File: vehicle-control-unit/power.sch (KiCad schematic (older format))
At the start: 0 parts

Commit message: Finish VCU schematic
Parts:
- added C1: 10u, symbol Device:CP
- added C2: 22u, symbol Device:CP
- added J13: Conn_01x02_Male, symbol Connector:Conn_01x02_Male
- added JP6: Jumper_3_Bridged12, symbol earth-rover-symbols:Jumper_3_Bridged12
- added R16: 820E, symbol Device:R
- added R17: 240E, symbol Device:R
- added RV1: 100E, symbol Device:R_POT_TRIM
- added SW1: SW_SPST, symbol Switch:SW_SPST
- added U4: MIC29502WT, Package_TO_SOT_THT:TO-220-5_P3.4x3.7mm_StaggerEven_Lead3.8mm_Vertical, symbol Regulator_Linear:MIC29502WT
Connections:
- new net: JP6.2 (C), U4.1 (EN)
- new net: RV1.2, U4.5 (ADJ)
- new net: R16.2, RV1.1
- new net: R17.1, RV1.3
- new net: JP6.1 (A), SW1.2 (B)
- new net +5V: C2.1, R16.1, U4.4 (VOUT)
- new net +BATT: C1.1, J13.1 (Pin_1), SW1.1 (A), U4.2 (VIN)
- new net BEC: JP6.3 (B)
- new net GND: C1.2, C2.2, J13.2 (Pin_2), R17.2, U4.3 (GND)
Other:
- note added: "Jumper selects switch or BEC\npower supply to switch power"

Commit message: Review schematics
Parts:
- added C7: 100n, symbol Device:C
- added R16: 2M, 1%, symbol Device:R
- added R17: 1M, 1%, symbol Device:R
- renumbered C1 to C6, C2 to C8, R16 to R18, R17 to R19
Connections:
- net +BATT: now also R16.1
- net GND: now also C7.2, R17.2
- new net BATTERY_MONITOR: C7.1, R16.2, R17.1
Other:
- note added: "Jumper selects switch\nor BEC power supply\nto switch VCU power"
- note removed: "Jumper selects switch or BEC\npower supply to switch power"
- moved on the sheet: C6, C8, J13, JP6, R18, R19, RV1, SW1, U4

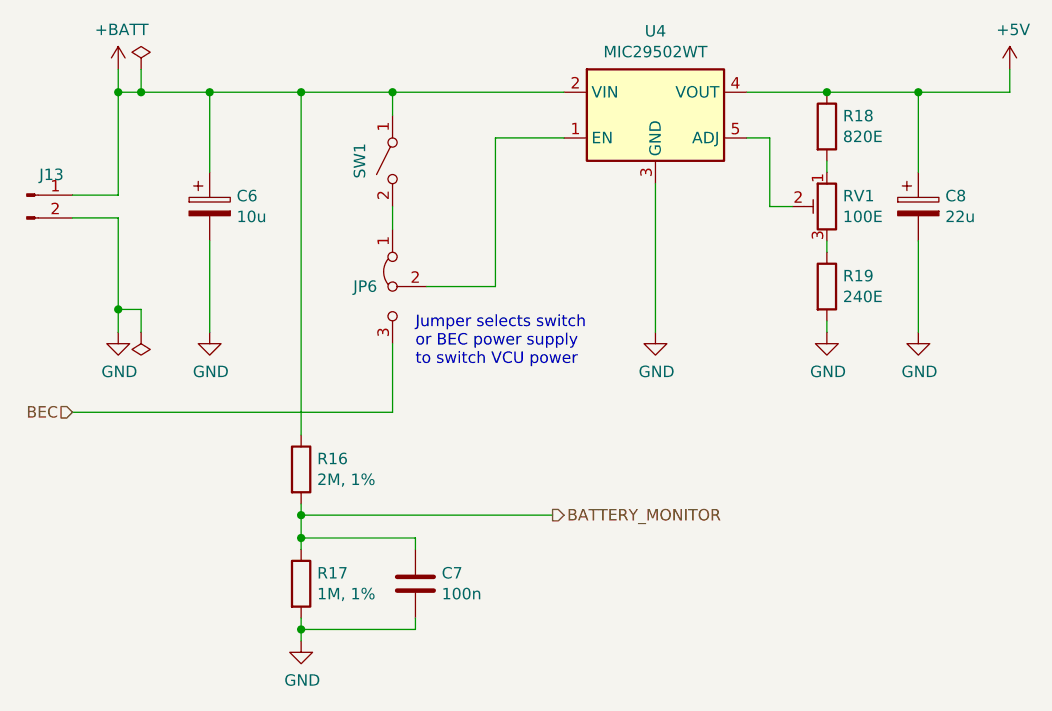
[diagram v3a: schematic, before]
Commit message: Correct resistor value for battery monitor
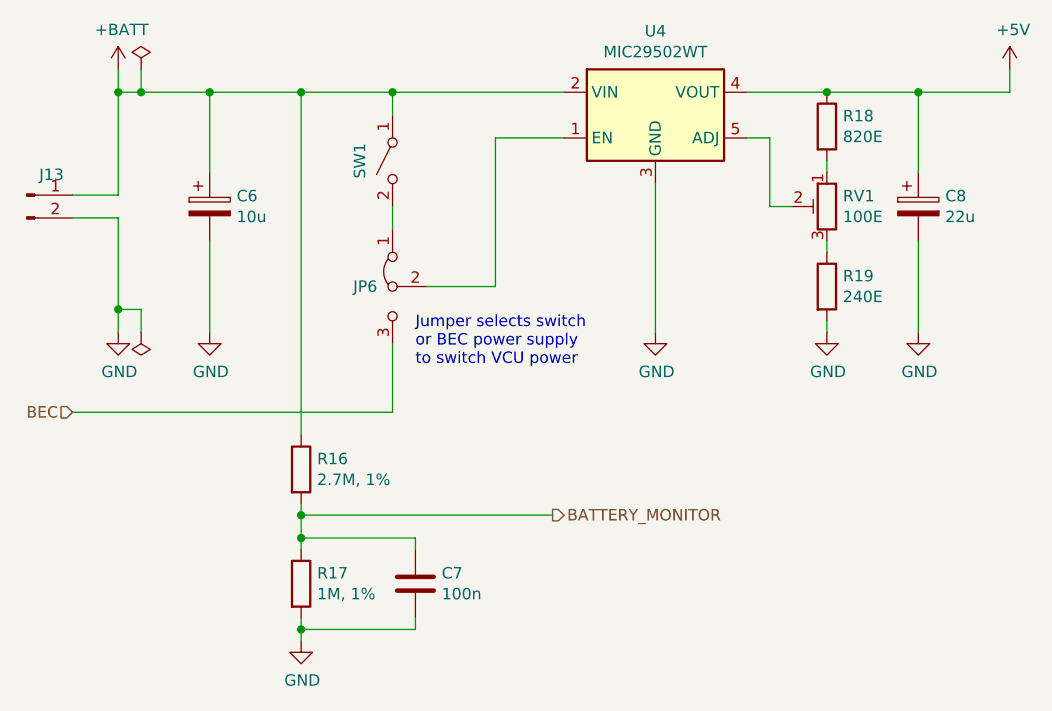
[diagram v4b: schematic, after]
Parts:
- R16: value 2M, 1% -> 2.7M, 1%
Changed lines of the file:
@@
 Sheet 3 3
 Title "Earth Rover"
-Date "2019-12-01"
-Rev "2"
+Date "2019-12-21"
+Rev "4"
 Comp "Vijfendertig BVBA"
 Comment1 "Maarten De Munck"
@@
 P 3350 8750
 F 0 "R16" H 3420 8796 50  0000 L CNN
-F 1 "2M, 1%" H 3420 8705 50  0000 L CNN
+F 1 "2.7M, 1%" H 3420 8705 50  0000 L CNN
 F 2 "" V 3280 8750 50  0001 C CNN
 F 3 "~" H 3350 8750 50  0001 C CNN

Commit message: Add pulldown resistor on MIC29502WT's EN input
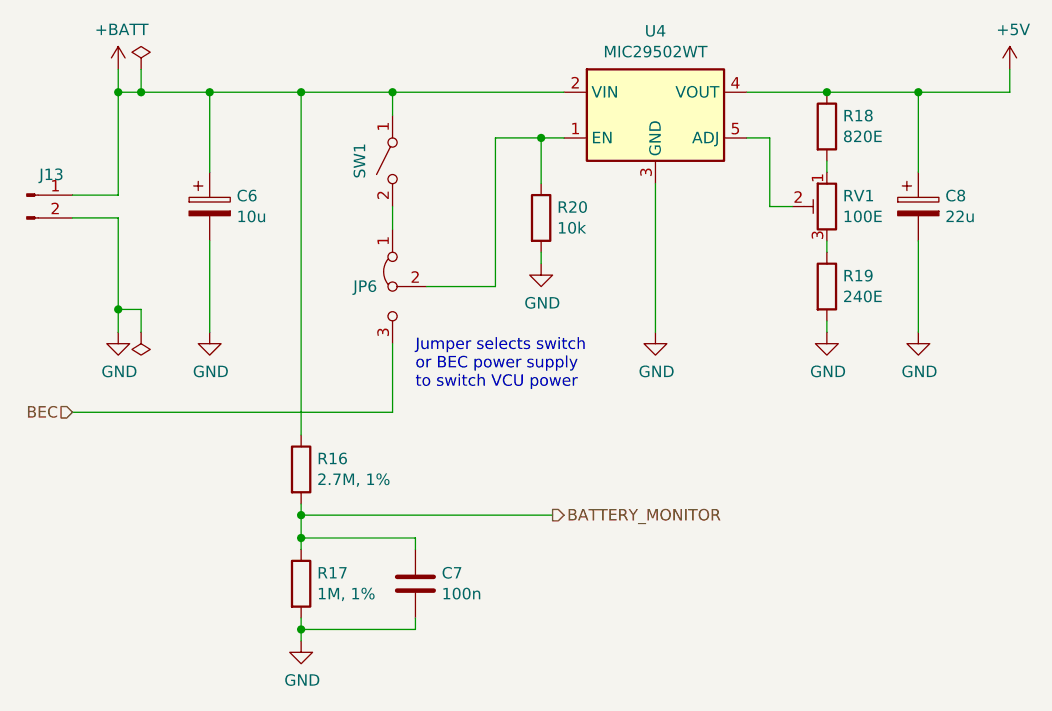
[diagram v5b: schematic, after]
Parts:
- added R20: 10k, symbol Device:R
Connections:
- net GND: now also R20.2
- net at JP6.2 (C), U4.1 (EN): now also R20.1
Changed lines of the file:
@@
 Wire Wire Line
 	2350 8500 3750 8500
-Text Notes 3850 8300 0    50   ~ 0
+Text Notes 3850 8400 0    50   ~ 0
 Jumper selects switch\nor BEC power supply\nto switch VCU power
 Wire Wire Line
-	4200 7300 4500 7300
+	4200 7300 4400 7300
 Wire Wire Line
 	4200 7950 4200 7300
@@
 Text HLabel 4450 8950 2    50   Output ~ 0
 BATTERY_MONITOR
+$Comp
+L Device:R R20
+U 1 1 5E349CEB
+P 4400 7650
+F 0 "R20" H 4470 7696 50  0000 L CNN
+F 1 "10k" H 4470 7605 50  0000 L CNN
+F 2 "" V 4330 7650 50  0001 C CNN
+F 3 "~" H 4400 7650 50  0001 C CNN
+	1    4400 7650
+	1    0    0    -1
+$EndComp
+$Comp
+L power:GND #PWR045
+U 1 1 5E34A716
+P 4400 7850
+F 0 "#PWR045" H 4400 7600 50  0001 C CNN
+F 1 "GND" H 4405 7677 50  0000 C CNN
+F 2 "" H 4400 7850 50  0001 C CNN
+F 3 "" H 4400 7850 50  0001 C CNN
+	1    4400 7850
+	1    0    0    -1
+$EndComp
+Wire Wire Line
+	4400 7850 4400 7800
+Wire Wire Line
+	4400 7500 4400 7300
+Connection ~ 4400 7300
+Wire Wire Line
+	4400 7300 4500 7300
 $EndSCHEMATC

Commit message: Fix some errors in the VCU hardware
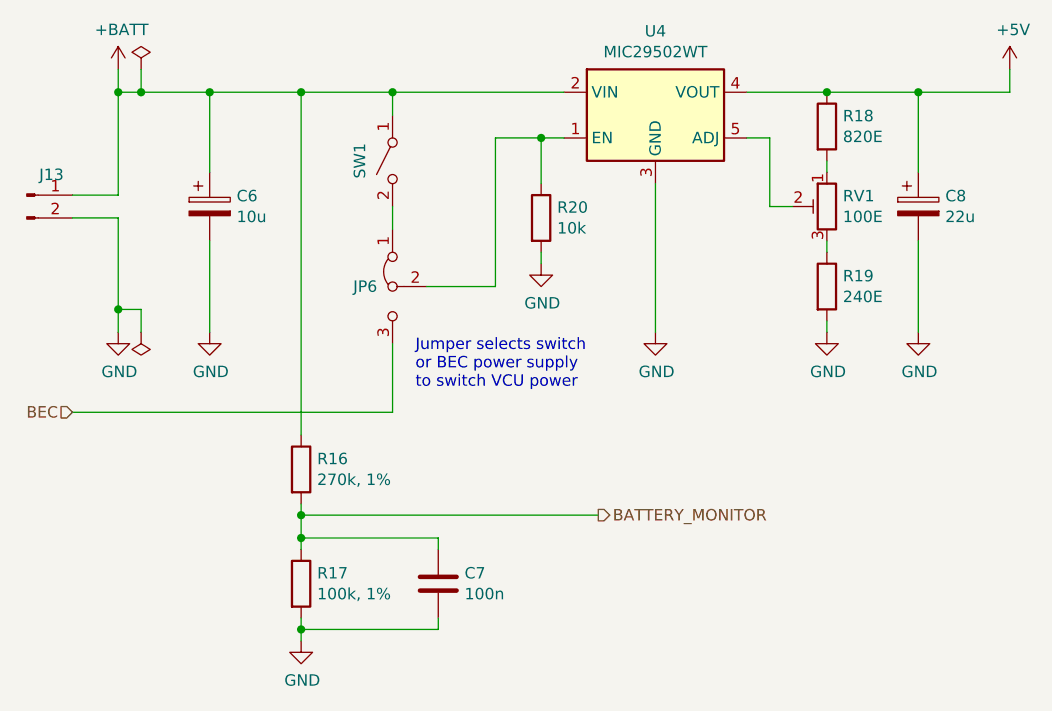
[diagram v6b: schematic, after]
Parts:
- R16: value 2.7M, 1% -> 270k, 1%
- R17: value 1M, 1% -> 100k, 1%
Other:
- moved on the sheet: C7
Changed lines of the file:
@@
 Sheet 3 3
 Title "Earth Rover"
-Date "2019-12-21"
-Rev "4"
+Date "2020-02-23"
+Rev "5"
 Comp "Vijfendertig BVBA"
 Comment1 "Maarten De Munck"
@@
 P 3350 8750
 F 0 "R16" H 3420 8796 50  0000 L CNN
-F 1 "2.7M, 1%" H 3420 8705 50  0000 L CNN
+F 1 "270k, 1%" H 3420 8705 50  0000 L CNN
 F 2 "" V 3280 8750 50  0001 C CNN
 F 3 "~" H 3350 8750 50  0001 C CNN
@@
 P 3350 9250
 F 0 "R17" H 3420 9296 50  0000 L CNN
-F 1 "1M, 1%" H 3420 9205 50  0000 L CNN
+F 1 "100k, 1%" H 3420 9205 50  0000 L CNN
 F 2 "" V 3280 9250 50  0001 C CNN
 F 3 "~" H 3350 9250 50  0001 C CNN
@@
 L Device:C C7
 U 1 1 5E015FEC
-P 3850 9250
-F 0 "C7" H 3965 9296 50  0000 L CNN
-F 1 "100n" H 3965 9205 50  0000 L CNN
-F 2 "" H 3888 9100 50  0001 C CNN
-F 3 "~" H 3850 9250 50  0001 C CNN
-	1    3850 9250
+P 3950 9250
+F 0 "C7" H 4065 9296 50  0000 L CNN
+F 1 "100n" H 4065 9205 50  0000 L CNN
+F 2 "" H 3988 9100 50  0001 C CNN
+F 3 "~" H 3950 9250 50  0001 C CNN
+	1    3950 9250
 	1    0    0    -1
 $EndComp
@@
 	3350 9100 3350 9050
 Wire Wire Line
-	3350 9050 3850 9050
-Wire Wire Line
-	3850 9050 3850 9100
+	3350 9050 3950 9050
+Wire Wire Line
+	3950 9050 3950 9100
 Connection ~ 3350 9050
 $Comp
@@
 	3350 9500 3350 9450
 Wire Wire Line
-	3350 9450 3850 9450
-Wire Wire Line
-	3850 9450 3850 9400
+	3350 9450 3950 9450
+Wire Wire Line
+	3950 9450 3950 9400
 Connection ~ 3350 9450
 Wire Wire Line
@@
 	3350 8900 3350 8950
 Wire Wire Line
-	3350 8950 4450 8950
+	3350 8950 4650 8950
 Connection ~ 3350 8950
 Wire Wire Line
 	3350 8950 3350 9050
-Text HLabel 4450 8950 2    50   Output ~ 0
-BATTERY_MONITOR
 $Comp
 L Device:R R20
@@
 Wire Wire Line
 	4400 7300 4500 7300
+Text HLabel 4650 8950 2    50   Output ~ 0
+BATTERY_MONITOR
 $EndSCHEMATC

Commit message: Wire all turn signal LEDs in parallel
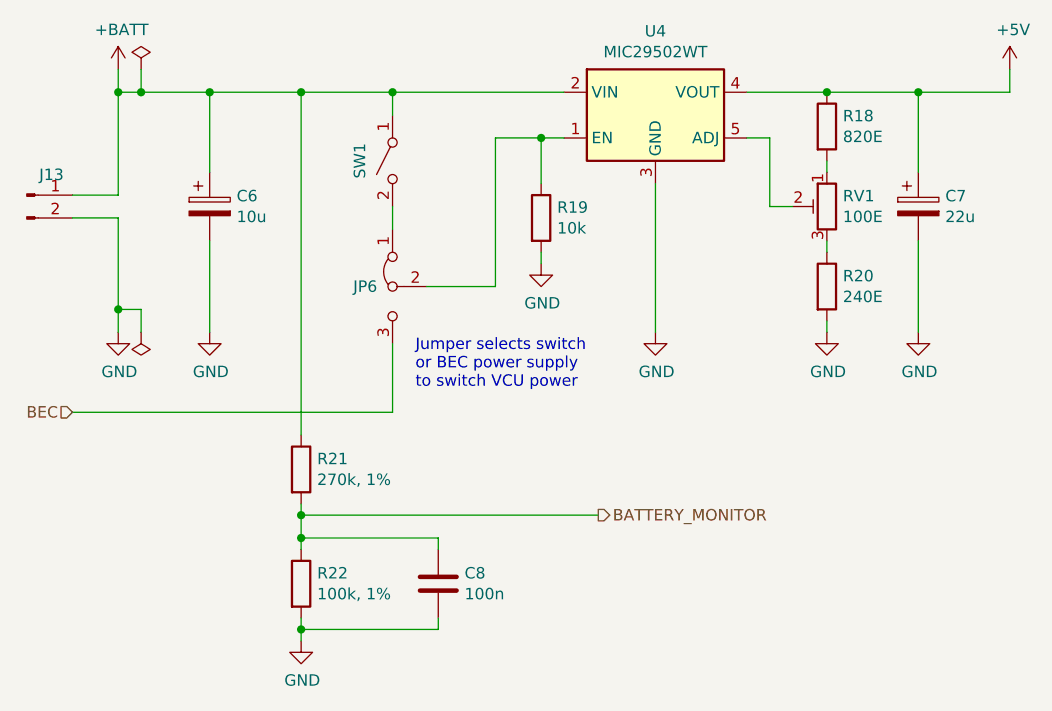
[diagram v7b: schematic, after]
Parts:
- renumbered C8 to C7, C7 to C8, R20 to R19, R19 to R20, R16 to R21, R17 to R22
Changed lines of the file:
@@
 Sheet 3 3
 Title "Earth Rover"
-Date "2020-02-23"
-Rev "5"
+Date "2020-04-25"
+Rev "6"
 Comp "Vijfendertig BVBA"
 Comment1 "Maarten De Munck"
@@
 $EndDescr
 $Comp
-L Device:R R16
+L Device:R R21
 U 1 1 5E01562C
 P 3350 8750
-F 0 "R16" H 3420 8796 50  0000 L CNN
+F 0 "R21" H 3420 8796 50  0000 L CNN
 F 1 "270k, 1%" H 3420 8705 50  0000 L CNN
 F 2 "" V 3280 8750 50  0001 C CNN
@@
 $EndComp
 $Comp
-L Device:R R17
+L Device:R R22
 U 1 1 5E015B81
 P 3350 9250
-F 0 "R17" H 3420 9296 50  0000 L CNN
+F 0 "R22" H 3420 9296 50  0000 L CNN
 F 1 "100k, 1%" H 3420 9205 50  0000 L CNN
 F 2 "" V 3280 9250 50  0001 C CNN
@@
 $EndComp
 $Comp
-L Device:C C7
+L Device:C C8
 U 1 1 5E015FEC
 P 3950 9250
-F 0 "C7" H 4065 9296 50  0000 L CNN
+F 0 "C8" H 4065 9296 50  0000 L CNN
 F 1 "100n" H 4065 9205 50  0000 L CNN
 F 2 "" H 3988 9100 50  0001 C CNN
@@
 Connection ~ 3350 9050
 $Comp
-L power:GND #PWR040
+L power:GND #PWR045
 U 1 1 5E01F8D8
 P 3350 9500
-F 0 "#PWR040" H 3350 9250 50  0001 C CNN
+F 0 "#PWR045" H 3350 9250 50  0001 C CNN
 F 1 "GND" H 3355 9327 50  0000 C CNN
 F 2 "" H 3350 9500 50  0001 C CNN
@@
 $EndComp
 $Comp
-L power:GND #PWR038
+L power:GND #PWR040
 U 1 1 5E4FCEBE
 P 2550 8150
-F 0 "#PWR038" H 2550 7900 50  0001 C CNN
+F 0 "#PWR040" H 2550 7900 50  0001 C CNN
 F 1 "GND" H 2555 7977 50  0000 C CNN
 F 2 "" H 2550 8150 50  0001 C CNN
@@
 $EndComp
 $Comp
-L power:GND #PWR039
+L power:GND #PWR041
 U 1 1 5E4FB89E
 P 2950 8150
-F 0 "#PWR039" H 2950 7900 50  0001 C CNN
+F 0 "#PWR041" H 2950 7900 50  0001 C CNN
 F 1 "GND" H 2955 7977 50  0000 C CNN
 F 2 "" H 2950 8150 50  0001 C CNN
@@
 	6050 8150 6050 7750
 $Comp
-L power:GND #PWR043
+L power:GND #PWR044
 U 1 1 5E50947F
 P 6050 8150
-F 0 "#PWR043" H 6050 7900 50  0001 C CNN
+F 0 "#PWR044" H 6050 7900 50  0001 C CNN
 F 1 "GND" H 6055 7977 50  0000 C CNN
 F 2 "" H 6050 8150 50  0001 C CNN
@@
 $EndComp
 $Comp
-L power:+5V #PWR044
+L power:+5V #PWR038
 U 1 1 5E4FD133
 P 6450 7000
-F 0 "#PWR044" H 6450 6850 50  0001 C CNN
+F 0 "#PWR038" H 6450 6850 50  0001 C CNN
 F 1 "+5V" H 6465 7173 50  0000 C CNN
 F 2 "" H 6450 7000 50  0001 C CNN
@@
 $EndComp
 $Comp
-L Device:CP C8
+L Device:CP C7
 U 1 1 5E4FBE0F
 P 6050 7600
-F 0 "C8" H 6168 7646 50  0000 L CNN
+F 0 "C7" H 6168 7646 50  0000 L CNN
 F 1 "22u" H 6168 7555 50  0000 L CNN
 F 2 "" H 6088 7450 50  0001 C CNN
@@
 $EndComp
 $Comp
-L power:GND #PWR041
+L power:GND #PWR042
 U 1 1 5E4FB653
 P 4900 8150
-F 0 "#PWR041" H 4900 7900 50  0001 C CNN
+F 0 "#PWR042" H 4900 7900 50  0001 C CNN
 F 1 "GND" H 4905 7977 50  0000 C CNN
 F 2 "" H 4900 8150 50  0001 C CNN
@@
 $EndComp
 $Comp
-L power:GND #PWR042
+L power:GND #PWR043
 U 1 1 5E4FB449
 P 5650 8150
-F 0 "#PWR042" H 5650 7900 50  0001 C CNN
+F 0 "#PWR043" H 5650 7900 50  0001 C CNN
 F 1 "GND" H 5655 7977 50  0000 C CNN
 F 2 "" H 5650 8150 50  0001 C CNN
@@
 $EndComp
 $Comp
-L Device:R R19
+L Device:R R20
 U 1 1 5E4FA94E
 P 5650 7950
-F 0 "R19" H 5720 7996 50  0000 L CNN
+F 0 "R20" H 5720 7996 50  0000 L CNN
 F 1 "240E" H 5720 7905 50  0000 L CNN
 F 2 "" V 5580 7950 50  0001 C CNN
@@
 	3350 8950 3350 9050
 $Comp
-L Device:R R20
+L Device:R R19
 U 1 1 5E349CEB
 P 4400 7650
-F 0 "R20" H 4470 7696 50  0000 L CNN
+F 0 "R19" H 4470 7696 50  0000 L CNN
 F 1 "10k" H 4470 7605 50  0000 L CNN
 F 2 "" V 4330 7650 50  0001 C CNN
@@
 $EndComp
 $Comp
-L power:GND #PWR045
+L power:GND #PWR039
 U 1 1 5E34A716
 P 4400 7850
-F 0 "#PWR045" H 4400 7600 50  0001 C CNN
+F 0 "#PWR039" H 4400 7600 50  0001 C CNN
 F 1 "GND" H 4405 7677 50  0000 C CNN
 F 2 "" H 4400 7850 50  0001 C CNN

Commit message: Assign footprints
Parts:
- C6, C7: footprint (none) -> Capacitor_THT:CP_Radial_D5.0mm_P2.50mm
- C8: footprint (none) -> Capacitor_THT:C_Disc_D5.0mm_W2.5mm_P5.00mm
- J13: footprint (none) -> TerminalBlock:TerminalBlock_bornier-2_P5.08mm
- JP6: footprint (none) -> Connector_PinHeader_2.54mm:PinHeader_1x03_P2.54mm_Vertical
- R18, R19, R20, R21, R22: footprint (none) -> Resistor_THT:R_Axial_DIN0207_L6.3mm_D2.5mm_P10.16mm_Horizontal
- RV1: footprint (none) -> Potentiometer_THT:Potentiometer_Bourns_3296W_Vertical
- SW1: footprint (none) -> Connector_PinHeader_2.54mm:PinHeader_1x02_P2.54mm_Horizontal
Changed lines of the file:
@@
 F 0 "R21" H 3420 8796 50  0000 L CNN
 F 1 "270k, 1%" H 3420 8705 50  0000 L CNN
-F 2 "" V 3280 8750 50  0001 C CNN
+F 2 "Resistor_THT:R_Axial_DIN0207_L6.3mm_D2.5mm_P10.16mm_Horizontal" V 3280 8750 50  0001 C CNN
 F 3 "~" H 3350 8750 50  0001 C CNN
 	1    3350 8750
@@
 F 0 "R22" H 3420 9296 50  0000 L CNN
 F 1 "100k, 1%" H 3420 9205 50  0000 L CNN
-F 2 "" V 3280 9250 50  0001 C CNN
+F 2 "Resistor_THT:R_Axial_DIN0207_L6.3mm_D2.5mm_P10.16mm_Horizontal" V 3280 9250 50  0001 C CNN
 F 3 "~" H 3350 9250 50  0001 C CNN
 	1    3350 9250
@@
 F 0 "C8" H 4065 9296 50  0000 L CNN
 F 1 "100n" H 4065 9205 50  0000 L CNN
-F 2 "" H 3988 9100 50  0001 C CNN
+F 2 "Capacitor_THT:C_Disc_D5.0mm_W2.5mm_P5.00mm" H 3988 9100 50  0001 C CNN
 F 3 "~" H 3950 9250 50  0001 C CNN
 	1    3950 9250
@@
 F 0 "J13" H 2258 7639 50  0000 C CNN
 F 1 "Conn_01x02_Male" H 2258 7640 50  0001 C CNN
-F 2 "" H 2150 7550 50  0001 C CNN
+F 2 "TerminalBlock:TerminalBlock_bornier-2_P5.08mm" H 2150 7550 50  0001 C CNN
 F 3 "~" H 2150 7550 50  0001 C CNN
 	1    2150 7550
@@
 F 0 "C6" H 3068 7646 50  0000 L CNN
 F 1 "10u" H 3068 7555 50  0000 L CNN
-F 2 "" H 2988 7450 50  0001 C CNN
+F 2 "Capacitor_THT:CP_Radial_D5.0mm_P2.50mm" H 2988 7450 50  0001 C CNN
 F 3 "~" H 2950 7600 50  0001 C CNN
 	1    2950 7600
@@
 F 0 "JP6" V 3750 8017 50  0000 L CNN
 F 1 "Jumper_3_Bridged12" V 3795 8017 50  0001 L CNN
-F 2 "" H 3750 7950 50  0001 C CNN
+F 2 "Connector_PinHeader_2.54mm:PinHeader_1x03_P2.54mm_Vertical" H 3750 7950 50  0001 C CNN
 F 3 "~" H 3750 7950 50  0001 C CNN
 	1    3750 7950
@@
 F 0 "SW1" H 3750 7543 50  0000 C CNN
 F 1 "SW_SPST" H 3750 7544 50  0001 C CNN
-F 2 "" H 3750 7400 50  0001 C CNN
+F 2 "Connector_PinHeader_2.54mm:PinHeader_1x02_P2.54mm_Horizontal" H 3750 7400 50  0001 C CNN
 F 3 "~" H 3750 7400 50  0001 C CNN
 	1    3750 7400
@@
 F 0 "C7" H 6168 7646 50  0000 L CNN
 F 1 "22u" H 6168 7555 50  0000 L CNN
-F 2 "" H 6088 7450 50  0001 C CNN
+F 2 "Capacitor_THT:CP_Radial_D5.0mm_P2.50mm" H 6088 7450 50  0001 C CNN
 F 3 "~" H 6050 7600 50  0001 C CNN
 	1    6050 7600
@@
 F 0 "RV1" H 5580 7646 50  0000 R CNN
 F 1 "100E" H 5580 7555 50  0000 R CNN
-F 2 "" H 5650 7600 50  0001 C CNN
+F 2 "Potentiometer_THT:Potentiometer_Bourns_3296W_Vertical" H 5650 7600 50  0001 C CNN
 F 3 "~" H 5650 7600 50  0001 C CNN
 	1    5650 7600
@@
 F 0 "R20" H 5720 7996 50  0000 L CNN
 F 1 "240E" H 5720 7905 50  0000 L CNN
-F 2 "" V 5580 7950 50  0001 C CNN
+F 2 "Resistor_THT:R_Axial_DIN0207_L6.3mm_D2.5mm_P10.16mm_Horizontal" V 5580 7950 50  0001 C CNN
 F 3 "~" H 5650 7950 50  0001 C CNN
 	1    5650 7950
@@
 F 0 "R18" H 5720 7296 50  0000 L CNN
 F 1 "820E" H 5720 7205 50  0000 L CNN
-F 2 "" V 5580 7250 50  0001 C CNN
+F 2 "Resistor_THT:R_Axial_DIN0207_L6.3mm_D2.5mm_P10.16mm_Horizontal" V 5580 7250 50  0001 C CNN
 F 3 "~" H 5650 7250 50  0001 C CNN
 	1    5650 7250
@@
 F 0 "R19" H 4470 7696 50  0000 L CNN
 F 1 "10k" H 4470 7605 50  0000 L CNN
-F 2 "" V 4330 7650 50  0001 C CNN
+F 2 "Resistor_THT:R_Axial_DIN0207_L6.3mm_D2.5mm_P10.16mm_Horizontal" V 4330 7650 50  0001 C CNN
 F 3 "~" H 4400 7650 50  0001 C CNN
 	1    4400 7650
